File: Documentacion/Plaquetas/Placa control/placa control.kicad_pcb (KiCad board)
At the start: 2 copper layers, 120.7 x 94.5 mm, 45 parts, among them J1 Conn_01x02_Male, J10 Conn_01x06_Female, J11 Conn_01x03_Male, J12 Conn_01x03_Male, J13 Conn_01x03_Male, J2 DB9_Female_MountingHoles, J3 Screw_Terminal_01x02, J4 Conn_01x06_Male, J5 Conn_01x02_Male, J6 Conn_01x04_Male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

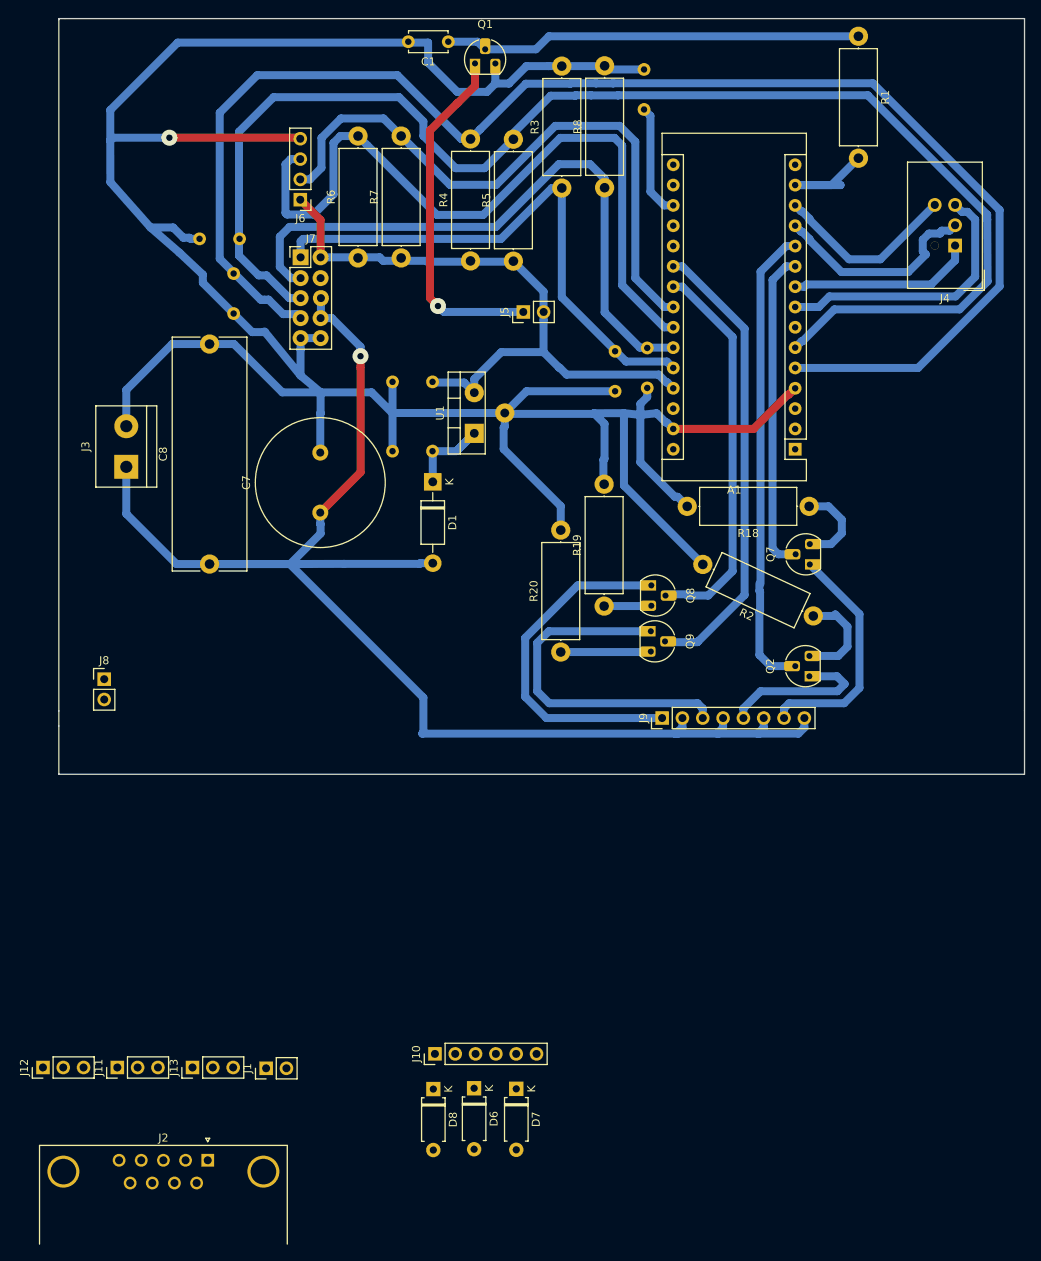
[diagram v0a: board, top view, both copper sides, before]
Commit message: Possible route design, swapped display connector pins
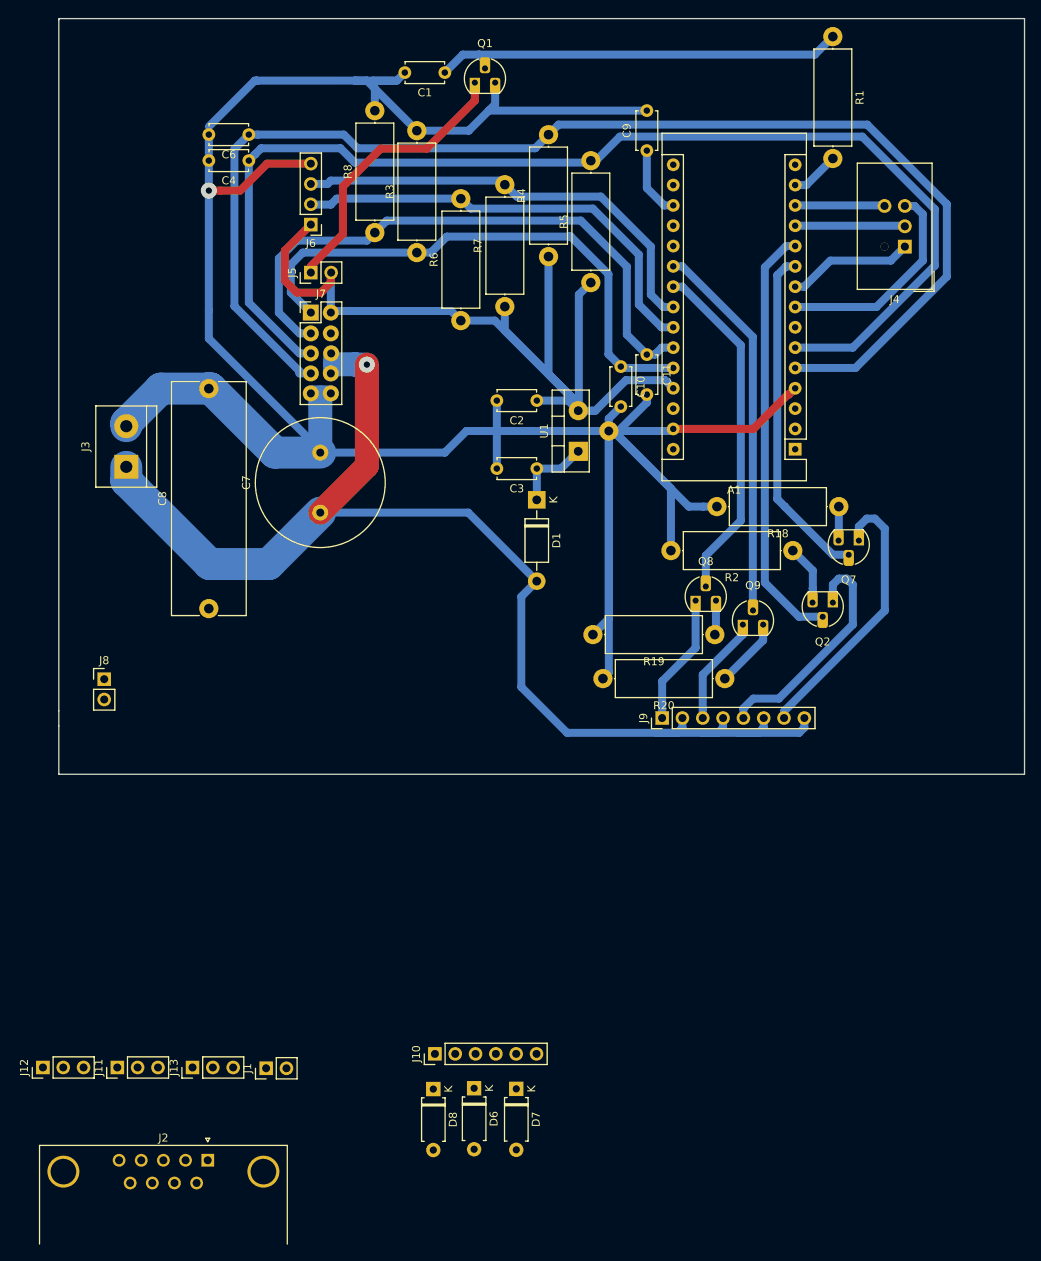
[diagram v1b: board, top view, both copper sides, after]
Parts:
- C10, C11, C2, C3, C4, C6, C9: moved to F.Cu
- moved R8 29.3 mm to (66.1, 53.5)
- moved J5 27.0 mm to (58.1, 58.5)
- moved R20 20.8 mm to (109.8, 109.3), turned to 180 degrees
- moved R3 19.8 mm to (71.3, 56.0)
- moved C6 17.5 mm to (50.3, 41.3), turned to 180 degrees
- moved R6 15.0 mm to (76.8, 64.5)
- moved R7 14.3 mm to (82.3, 62.8)
- moved R19 14.3 mm to (108.6, 103.8), turned to 180 degrees
- moved C2 13.2 mm to (86.3, 74.5)
- moved C3 13.2 mm to (86.3, 83.0)
- moved D1 13.2 mm to (86.3, 87.0)
- moved U1 13.2 mm to (91.5, 80.9)
- moved Q9 11.1 mm to (112.1, 102.0), turned to 0 degrees
- moved R5 10.0 mm to (93.1, 59.8)
- moved C4 9.85 mm to (50.3, 44.5)
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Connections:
- J6 pad 2: SDA-DISPLAY -> SCL-DISPLAY
- J6 pad 3: SCL-DISPLAY -> SDA-DISPLAY
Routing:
- net REF_5: track 81.6 -> 130.4 mm
- net SCL-DISPLAY: track 92.7 -> 56.0 mm
- net Net-(J9-Pad3): track 43.8 -> 13.8 mm
- net Net-(J9-Pad1): track 44.1 -> 16.4 mm
- net VCC: track 181.2 -> 157.6 mm
- net SDA-DISPLAY: track 77.8 -> 55.5 mm
- net SENSOR_FAN: track 171.1 -> 149.3 mm
- net SENSOR_PUMP: track 183.0 -> 161.4 mm
- net PWM_CALOR: track 26.6 -> 13.7 mm
- net PWM_FRIO: track 23.1 -> 11.2 mm
- net PIN-WARNING-LED-RED: track 57.9 -> 47.9 mm
- net Net-(J9-Pad5): track 19.9 -> 29.6 mm
- net BUZZER: track 15.0 -> 6.09 mm
- net GND: track 359.6 -> 350.7 mm
- net Net-(J5-Pad1): track 44.1 -> 35.6 mm, vias 1 -> 0
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
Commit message: Changed pump and fan sensor pins, routed accordingly, shrunk board size
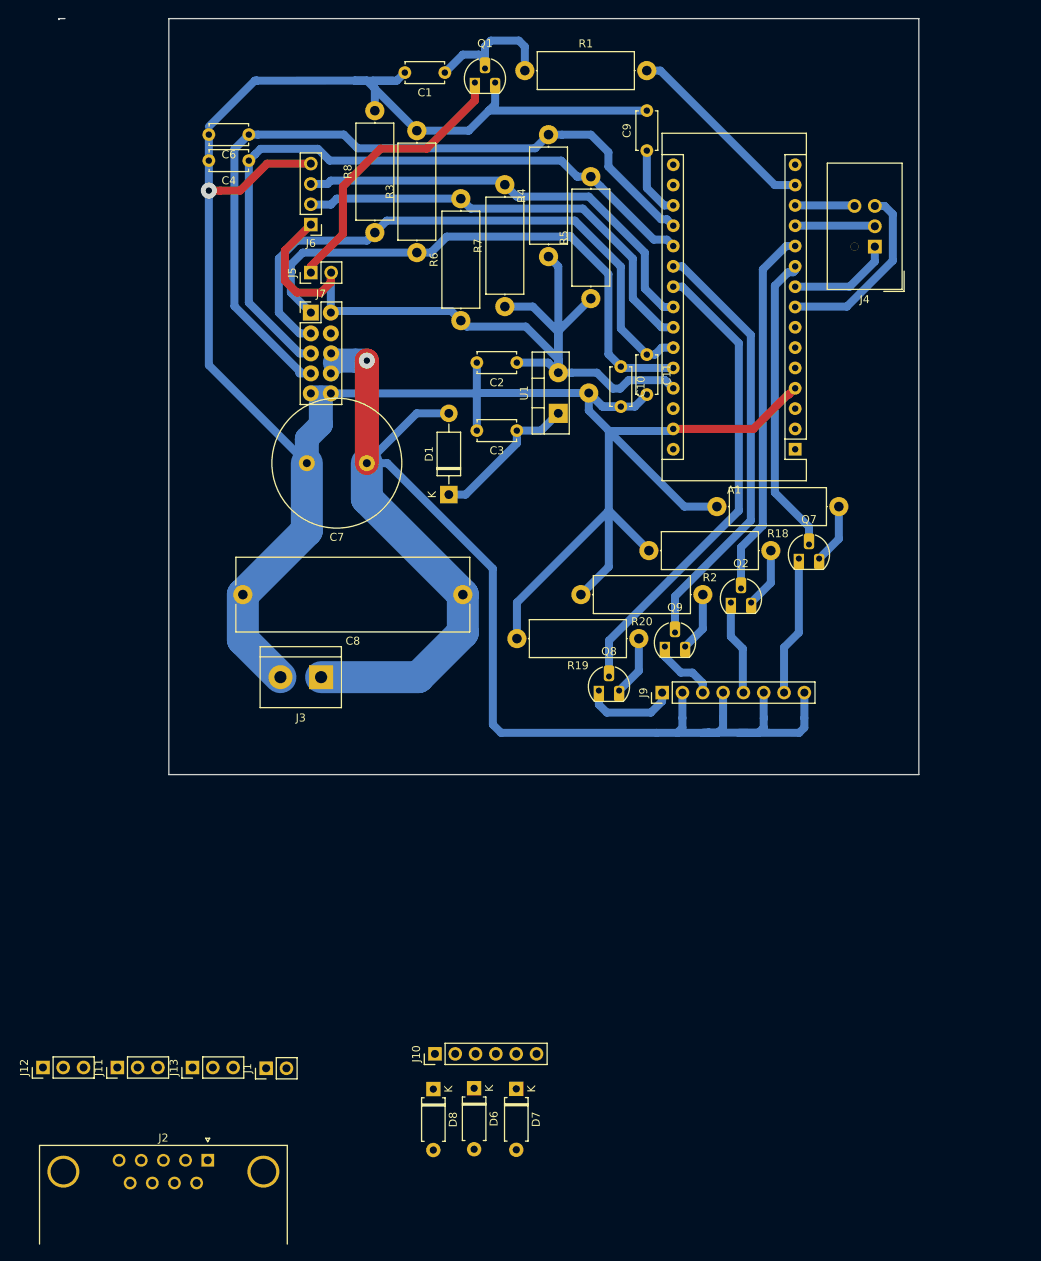
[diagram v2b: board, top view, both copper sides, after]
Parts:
- removed J8: Conn_01x02_Male, Connector_PinHeader_2.54mm:PinHeader_1x02_P2.54mm_Vertical
- moved R1 38.7 mm to (84.8, 33.3), turned to 0 degrees
- moved J3 35.8 mm to (59.4, 109.1), turned to 180 degrees
- moved C8 31.8 mm to (77.1, 98.8), turned to 180 degrees
- moved Q8 16.5 mm to (94.1, 110.3)
- moved Q2 12.8 mm to (110.6, 99.3), turned to 0 degrees
- moved D1 11.0 mm to (75.3, 86.3), turned to 90 degrees
- moved R20 10.9 mm to (107.1, 98.8)
- moved Q9 10.1 mm to (102.3, 104.8)
- moved R19 9.51 mm to (99.1, 104.3)
- moved C7 8.49 mm to (65.1, 82.4), turned to 180 degrees
- moved Q7 7.60 mm to (119.1, 93.8), turned to 0 degrees
- moved C2 5.37 mm to (83.8, 69.8)
- moved C3 5.37 mm to (83.8, 78.3)
- moved U1 5.37 mm to (89.0, 76.1)
- moved J4 3.75 mm to (128.6, 55.3)
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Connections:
- A1 pad 19: Net-(A1-Pad19) -> SENSOR_PUMP
- A1 pad 20: Net-(A1-Pad20) -> SENSOR_FAN
- A1 pad 5: SENSOR_PUMP -> Net-(A1-Pad5)
- A1 pad 6: SENSOR_FAN -> Net-(A1-Pad6)
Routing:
- net SENSOR_PUMP: track 161.4 -> 95.6 mm
- net SENSOR_FAN: track 149.3 -> 86.8 mm
- net Net-(C1-Pad1): track 51.5 -> 17.6 mm
- net VCC: track 157.6 -> 184.4 mm
- net BUZZER: track 6.09 -> 24.5 mm
- net GND: track 350.7 -> 332.9 mm
- net Net-(J9-Pad5): track 29.6 -> 11.9 mm
- net Net-(J9-Pad7): track 34.8 -> 17.5 mm
- net PIN-READY-LED-GREEN: track 43.4 -> 59.5 mm
- net REF_5: track 130.4 -> 115.0 mm
- net Net-(C3-Pad1): track 9.99 -> 18.8 mm
- net PIN-COLD-LED-BLUE: track 53.3 -> 46.3 mm
- net PIN-WARNING-LED-RED: track 47.9 -> 54.4 mm
- net Net-(J9-Pad3): track 13.8 -> 8.56 mm
- net Net-(J9-Pad1): track 16.4 -> 11.7 mm
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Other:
- board size 120.7 x 94.5 mm -> 107.5 x 94.5 mm

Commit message: Possible design, swapped sda and scl connector pins
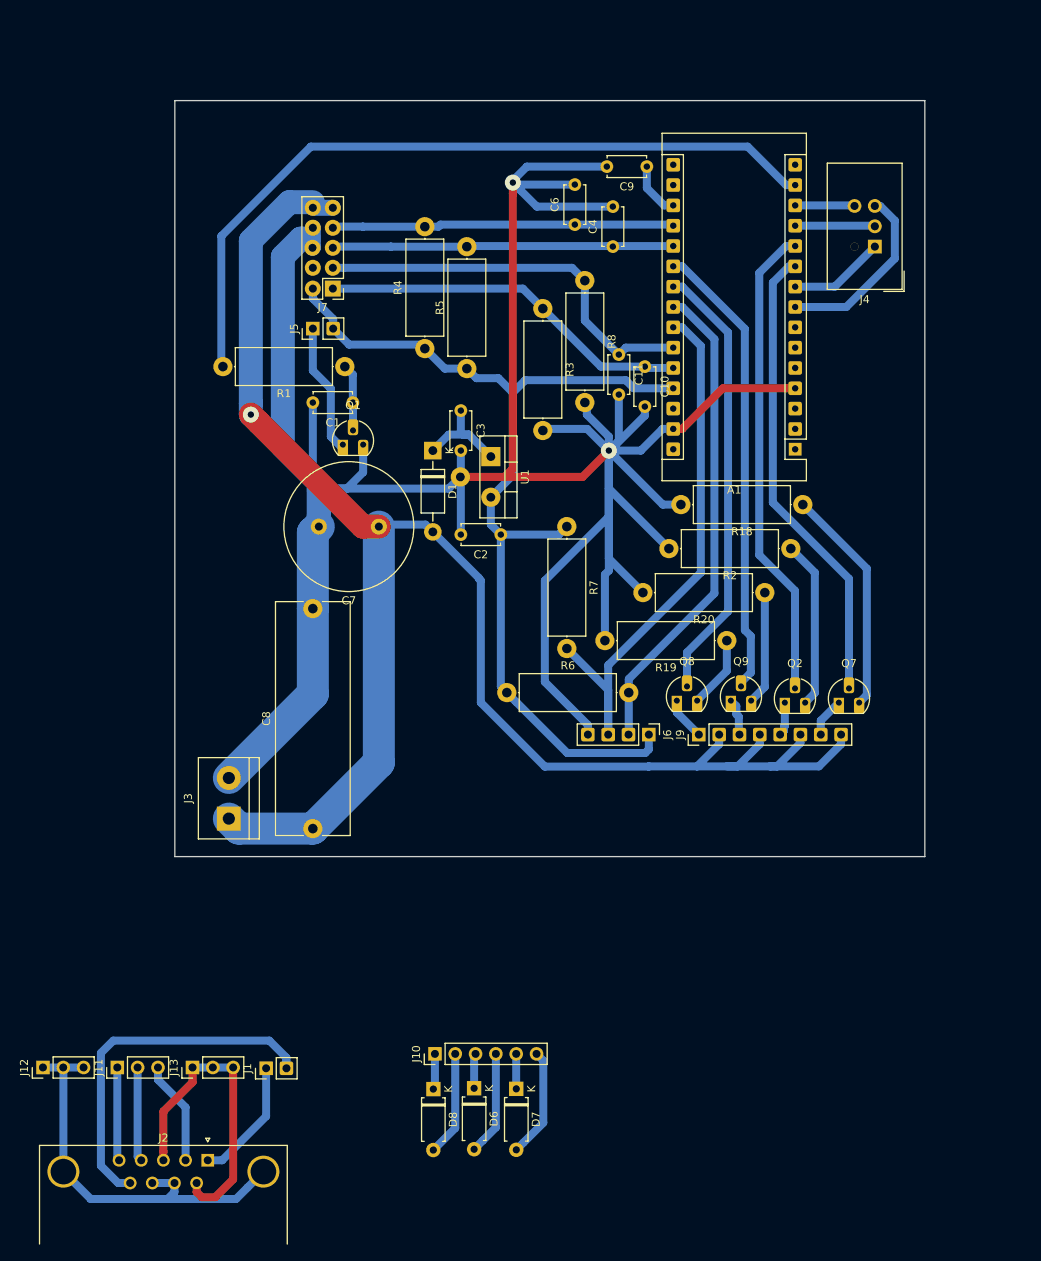
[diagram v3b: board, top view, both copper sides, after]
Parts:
- A1: footprint Module:Arduino_Nano -> custom_footprints:Arduino_Nano
- J1, J5: footprint Connector_PinHeader_2.54mm:PinHeader_1x02_P2.54mm_Vertical -> custom_footprints:PinHeader_1x02_P2.54mm_Vertical
- J6: footprint Connector_PinHeader_2.54mm:PinHeader_1x04_P2.54mm_Vertical -> custom_footprints:PinHeader_1x04_P2.54mm_Vertical
- J9: footprint Connector_PinHeader_2.54mm:PinHeader_1x08_P2.54mm_Vertical -> custom_footprints:PinHeader_1x08_P2.54mm_Vertical
- moved J6 76.5 mm to (100.3, 116.3), turned to 270 degrees
- moved Q1 48.2 mm to (62.1, 79.5)
- moved R6 46.9 mm to (82.6, 111.0), turned to 0 degrees
- moved C4 46.8 mm to (95.8, 55.3), turned to 90 degrees
- moved R1 43.3 mm to (62.3, 70.3), turned to 180 degrees
- moved C1 42.8 mm to (63.3, 74.8)
- moved C6 42.3 mm to (91.1, 52.5), turned to 90 degrees
- moved C8 34.7 mm to (58.3, 128.0), turned to 90 degrees
- moved R7 28.6 mm to (90.1, 90.3), turned to 270 degrees
- moved R8 26.9 mm to (92.3, 59.5), turned to 270 degrees
- moved C2 21.6 mm to (81.8, 91.3)
- moved J3 21.1 mm to (47.8, 126.8), turned to 90 degrees
- moved R4 19.3 mm to (72.3, 68.0)
- moved Q7 18.7 mm to (124.1, 111.8)
- moved R5 17.8 mm to (77.6, 70.5)
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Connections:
- J6 pad 2: SCL-DISPLAY -> SDA-DISPLAY
- J6 pad 3: SDA-DISPLAY -> SCL-DISPLAY
- J7 pad 5: GND -> VCC
- J7 pad 6: GND -> VCC
- J7 pad 7: VCC -> GND
- J7 pad 8: VCC -> GND
- R6 pad 2: SCL-DISPLAY -> SDA-DISPLAY
- R7 pad 2: SDA-DISPLAY -> SCL-DISPLAY
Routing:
- net BUZZER: track 24.5 -> 94.8 mm
- net GND: track 332.9 -> 398.8 mm, vias 1 -> 2
- net GND_C: track 0.00 -> 60.7 mm
- net SENSOR_PUMP: track 95.6 -> 42.8 mm
- net pump_sensor_C: track 0.00 -> 44.7 mm
- net SENSOR_FAN: track 86.8 -> 42.6 mm
- net VCC_C: track 0.00 -> 39.1 mm
- net PIN_SENSOR_TEMPERATURA_1: track 74.9 -> 50.3 mm
- net VCC: track 184.4 -> 207.5 mm
- net PIN_SENSOR_TEMPERATURA_2: track 69.0 -> 46.7 mm
- net Net-(Q7-Pad3): track 7.52 -> 28.5 mm
- net PIN-HOT-LED-YELLOW: track 37.9 -> 58.3 mm
- net Net-(J5-Pad1): track 35.6 -> 16.6 mm
- net fan_sensor_C: track 0.00 -> 15.6 mm
- net SCL-DISPLAY: track 55.2 -> 70.7 mm
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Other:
- board size 107.5 x 94.5 mm -> 93.8 x 94.5 mm
- net class Arduino added: clearance 0.7, trace_width 1, via_dia 2, via_drill 0.8
- net class Conector added: clearance 0.5, trace_width 1, via_dia 2, via_drill 0.8
- net class Default: clearance 0.5 -> 0.7
- rule trace_clearance: 0.5 -> 0.7
